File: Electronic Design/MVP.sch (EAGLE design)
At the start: 38 parts, among them IC1 ACS711KLCTR-12AB-T, IC3 ATMEGA328-PU, Q2 16MHz, Q3 IRF9540, Q4 IRF9540

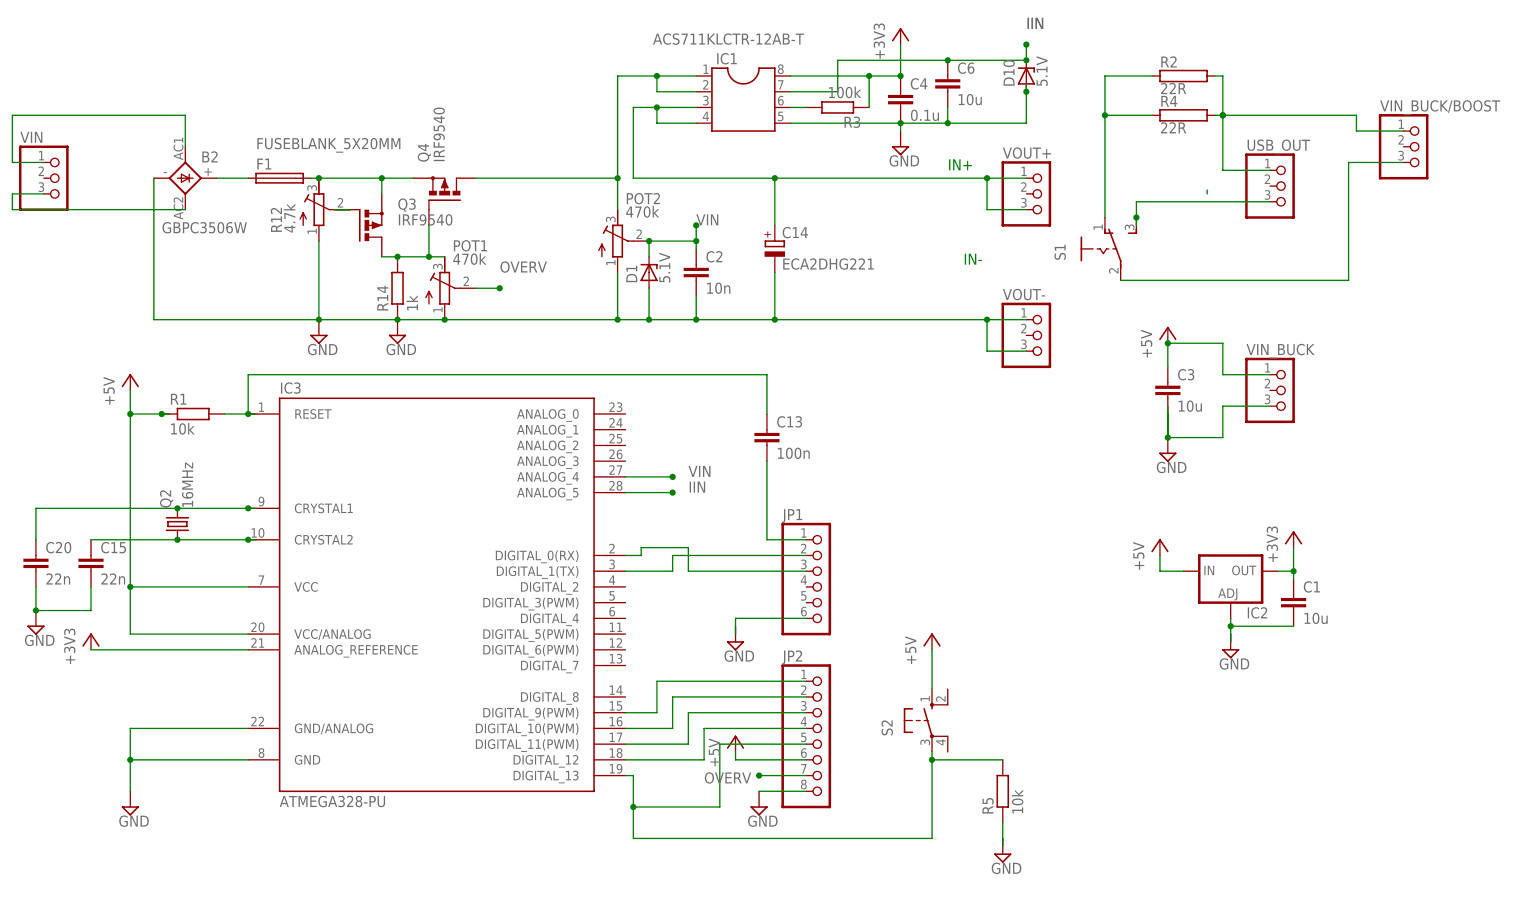
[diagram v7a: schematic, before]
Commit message: Change some components connections in schematics and update board layout
changed top and bottom layer isolation to 0.3
completed unrouted wires
rerouted Output to come from capacitor directly
moved +3V3 near POT2 to allow more space forground trace to penetrate to C1 and C2
moved decoupling caps C4 and C1 closer to IC1 and IC3, respectively
added several ground stitching vias between top and bottom layer
increased some corner sizes
rerouted +5V from under IC4 to go through decoupling cap C3
connected R5 to GND
connected JP1 to GND
mirrored POT1 to allow easier routing
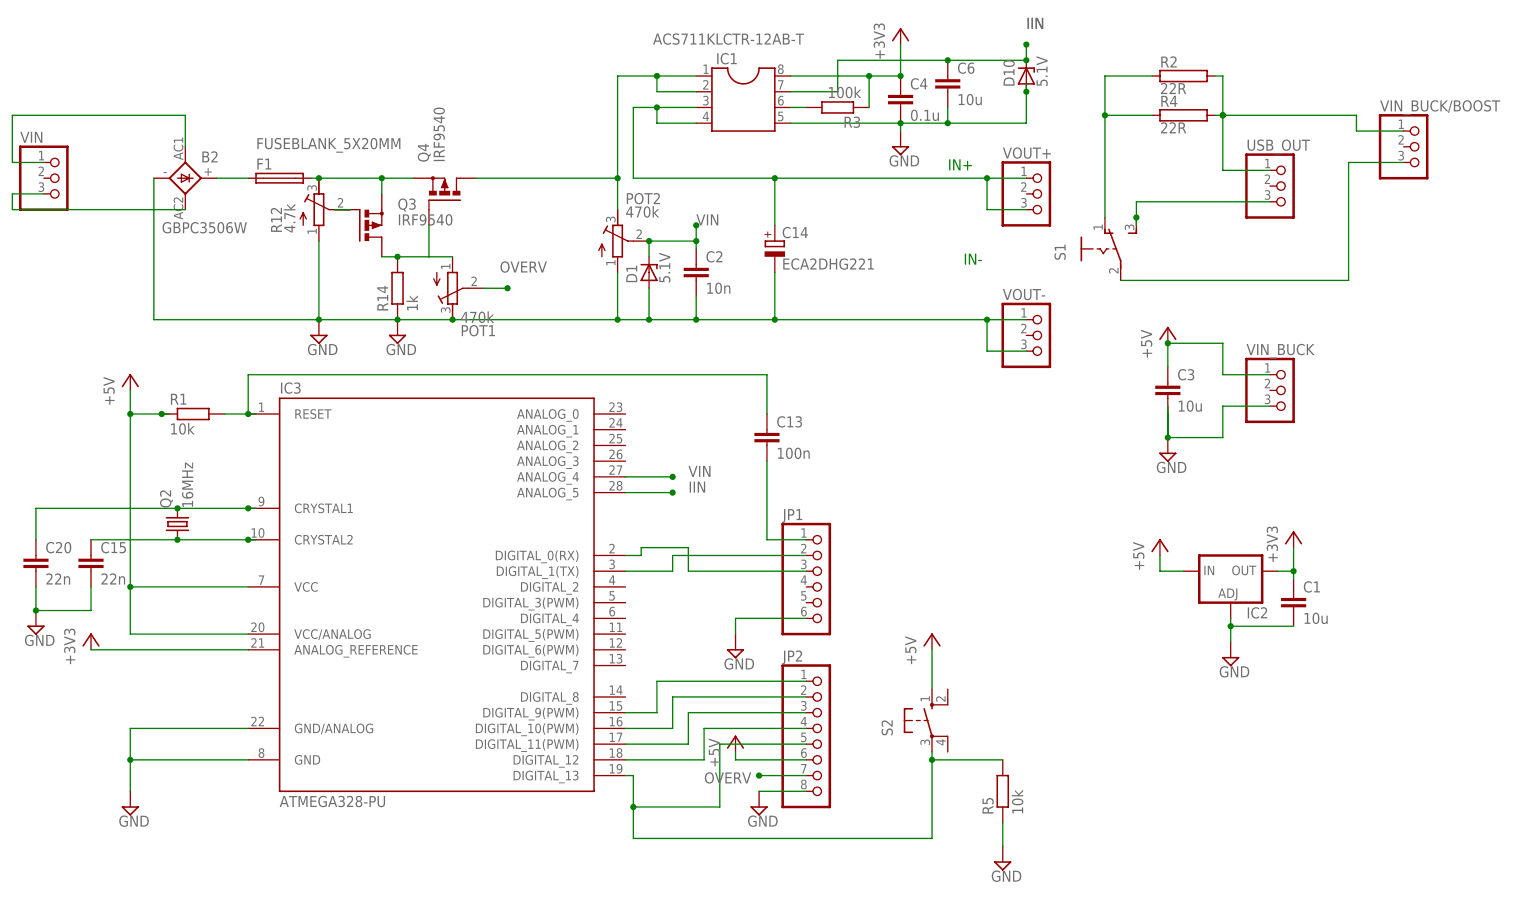
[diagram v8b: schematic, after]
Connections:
- removed net N$21: JP1.6
- removed net N$26: R5.1
- net GND: now also JP1.6, POT1.E, R5.1; no longer POT1.A
- net N$35: now also POT1.A; no longer POT1.E
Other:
- moved on the sheet: POT1
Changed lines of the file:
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@@
 <?xml version="1.0" encoding="utf-8"?>
 <!DOCTYPE eagle SYSTEM "eagle.dtd">
-<eagle version="7.5.0">
+<eagle version="7.6.0">
 <drawing>
 <settings>
@@
 <setting verticaltext="up"/>
 </settings>
-<grid distance="0.1" unitdist="inch" unit="inch" style="lines" multiple="1" display="no" altdistance="0.01" altunitdist="inch" altunit="inch"/>
+<grid distance="0.05" unitdist="inch" unit="inch" style="lines" multiple="1" display="no" altdistance="0.01" altunitdist="inch" altunit="inch"/>
 <layers>
 <layer number="1" name="Top" color="4" fill="1" visible="no" active="no"/>
@@
 <instance part="+3V2" gate="1" x="74.93" y="64.77"/>
 <instance part="IC2" gate="G$1" x="85.09" y="25.4"/>
-<instance part="SUPPLY5" gate="GND" x="85.09" y="12.7"/>
+<instance part="SUPPLY5" gate="GND" x="85.09" y="11.43"/>
 <instance part="+3V3" gate="1" x="73.66" y="30.48"/>
 <instance part="+3V4" gate="G$1" x="95.25" y="31.75"/>
@@
 <instance part="+3V5" gate="G$1" x="-99.06" y="15.24"/>
 <instance part="JP1" gate="A" x="19.05" y="22.86"/>
-<instance part="SUPPLY6" gate="GND" x="5.08" y="13.97"/>
+<instance part="SUPPLY6" gate="GND" x="5.08" y="12.7"/>
 <instance part="C3" gate="G$1" x="74.93" y="55.88"/>
 <instance part="VIN_BUCK/BOOST" gate="A" x="115.57" y="93.98"/>
@@
 <instance part="+5V2" gate="1" x="36.83" y="15.24"/>
 <instance part="R5" gate="G$1" x="48.26" y="-10.16" rot="R90"/>
-<instance part="SUPPLY3" gate="GND" x="48.26" y="-20.32"/>
+<instance part="SUPPLY3" gate="GND" x="48.26" y="-21.59"/>
 <instance part="+5V3" gate="1" x="5.08" y="-1.27"/>
-<instance part="POT1" gate="G$1" x="-41.91" y="71.12" smashed="yes">
-<attribute name="NAME" x="-40.64" y="77.089" size="1.778" layer="95"/>
-<attribute name="VALUE" x="-40.64" y="74.93" size="1.778" layer="96"/>
+<instance part="POT1" gate="G$1" x="-40.64" y="71.12" smashed="yes" rot="MR180">
+<attribute name="NAME" x="-39.37" y="65.151" size="1.778" layer="95" rot="MR180"/>
+<attribute name="VALUE" x="-39.37" y="67.31" size="1.778" layer="96" rot="MR180"/>
 </instance>
 <instance part="D1" gate="G$1" x="-8.89" y="73.66" rot="R90"/>
@@
 <junction x="45.72" y="66.04"/>
 <junction x="11.43" y="66.04"/>
-<wire x1="-49.53" y1="66.04" x2="-41.91" y2="66.04" width="0.1524" layer="91"/>
-<wire x1="-41.91" y1="66.04" x2="-13.97" y2="66.04" width="0.1524" layer="91"/>
 <wire x1="-13.97" y1="66.04" x2="-8.89" y2="66.04" width="0.1524" layer="91"/>
 <wire x1="-8.89" y1="66.04" x2="-1.27" y2="66.04" width="0.1524" layer="91"/>
@@
 <junction x="-8.89" y="66.04"/>
 <junction x="-1.27" y="66.04"/>
-<pinref part="POT1" gate="G$1" pin="A"/>
-<junction x="-41.91" y="66.04"/>
 <pinref part="D1" gate="G$1" pin="A"/>
+<wire x1="-49.53" y1="66.04" x2="-40.64" y2="66.04" width="0.1524" layer="91"/>
+<wire x1="-40.64" y1="66.04" x2="-13.97" y2="66.04" width="0.1524" layer="91"/>
+<pinref part="POT1" gate="G$1" pin="E"/>
+<junction x="-40.64" y="66.04"/>
 </segment>
 <segment>
@@
 <wire x1="85.09" y1="17.78" x2="85.09" y2="16.51" width="0.1524" layer="91"/>
 <pinref part="C1" gate="G$1" pin="2"/>
-<wire x1="85.09" y1="16.51" x2="85.09" y2="15.24" width="0.1524" layer="91"/>
-<wire x1="85.09" y1="15.24" x2="85.09" y2="13.97" width="0.1524" layer="91"/>
+<wire x1="85.09" y1="16.51" x2="85.09" y2="13.97" width="0.1524" layer="91"/>
 <wire x1="95.25" y1="16.51" x2="85.09" y2="16.51" width="0.1524" layer="91"/>
 <junction x="85.09" y="16.51"/>
@@
 <pinref part="SUPPLY17" gate="GND" pin="GND"/>
 <wire x1="16.51" y1="-10.16" x2="8.89" y2="-10.16" width="0.1524" layer="91"/>
+</segment>
+<segment>
+<pinref part="R5" gate="G$1" pin="1"/>
+<wire x1="48.26" y1="-15.24" x2="48.26" y2="-19.05" width="0.1524" layer="91"/>
+<pinref part="SUPPLY3" gate="GND" pin="GND"/>
+</segment>
+<segment>
+<pinref part="JP1" gate="A" pin="6"/>
+<wire x1="16.51" y1="17.78" x2="5.08" y2="17.78" width="0.1524" layer="91"/>
+<wire x1="5.08" y1="17.78" x2="5.08" y2="15.24" width="0.1524" layer="91"/>
+<pinref part="SUPPLY6" gate="GND" pin="GND"/>
 </segment>
 </net>
@@
 <wire x1="-44.45" y1="76.2" x2="-44.45" y2="81.28" width="0.1524" layer="91"/>
 <junction x="-49.53" y="76.2"/>
-<pinref part="POT1" gate="G$1" pin="E"/>
-<wire x1="-44.45" y1="76.2" x2="-41.91" y2="76.2" width="0.1524" layer="91"/>
-<junction x="-44.45" y="76.2"/>
+<pinref part="POT1" gate="G$1" pin="A"/>
+<wire x1="-40.64" y1="76.2" x2="-44.45" y2="76.2" width="0.1524" layer="91"/>
 </segment>
 </net>
@@
 </segment>
 </net>
-<net name="N$18" class="0">
-<segment>
-<wire x1="81.28" y1="86.995" x2="81.28" y2="86.36" width="0.1524" layer="91"/>
-</segment>
-</net>
 <net name="+3V3" class="0">
 <segment>
@@
 <wire x1="16.51" y1="30.48" x2="10.16" y2="30.48" width="0.1524" layer="91"/>
 <wire x1="10.16" y1="30.48" x2="10.16" y2="43.18" width="0.1524" layer="91"/>
-</segment>
-</net>
-<net name="N$21" class="0">
-<segment>
-<pinref part="JP1" gate="A" pin="6"/>
-<wire x1="16.51" y1="17.78" x2="5.08" y2="17.78" width="0.1524" layer="91"/>
-<wire x1="5.08" y1="17.78" x2="5.08" y2="15.24" width="0.1524" layer="91"/>
 </segment>
 </net>
@@
 </segment>
 </net>
-<net name="N$26" class="0">
-<segment>
-<pinref part="R5" gate="G$1" pin="1"/>
-<wire x1="48.26" y1="-15.24" x2="48.26" y2="-19.05" width="0.1524" layer="91"/>
-</segment>
-</net>
 <net name="N$6" class="0">
 <segment>
@@
 <segment>
 <pinref part="POT1" gate="G$1" pin="S"/>
-<wire x1="-36.83" y1="71.12" x2="-33.02" y2="71.12" width="0.1524" layer="91"/>
-<junction x="-33.02" y="71.12"/>
+<wire x1="-35.56" y1="71.12" x2="-31.75" y2="71.12" width="0.1524" layer="91"/>
+<junction x="-31.75" y="71.12"/>
 <label x="-33.02" y="73.66" size="1.778" layer="95"/>
 </segment>
